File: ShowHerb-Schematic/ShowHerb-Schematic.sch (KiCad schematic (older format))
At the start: 7 parts

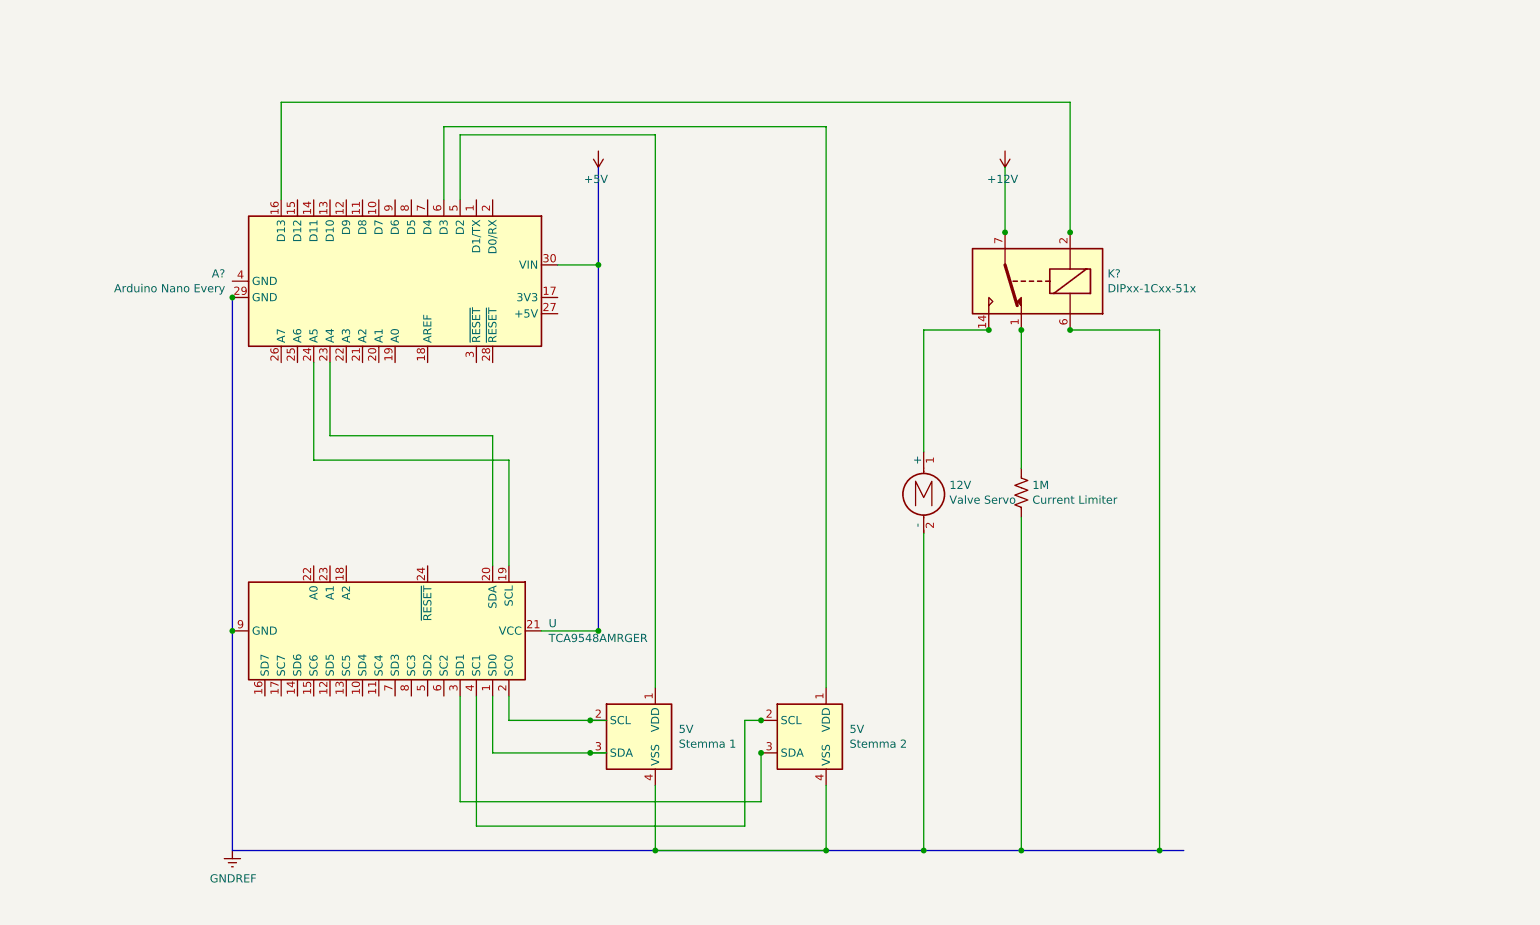
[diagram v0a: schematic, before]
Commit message: Added rain sensor and photoresistor to schematic, v2 storage box
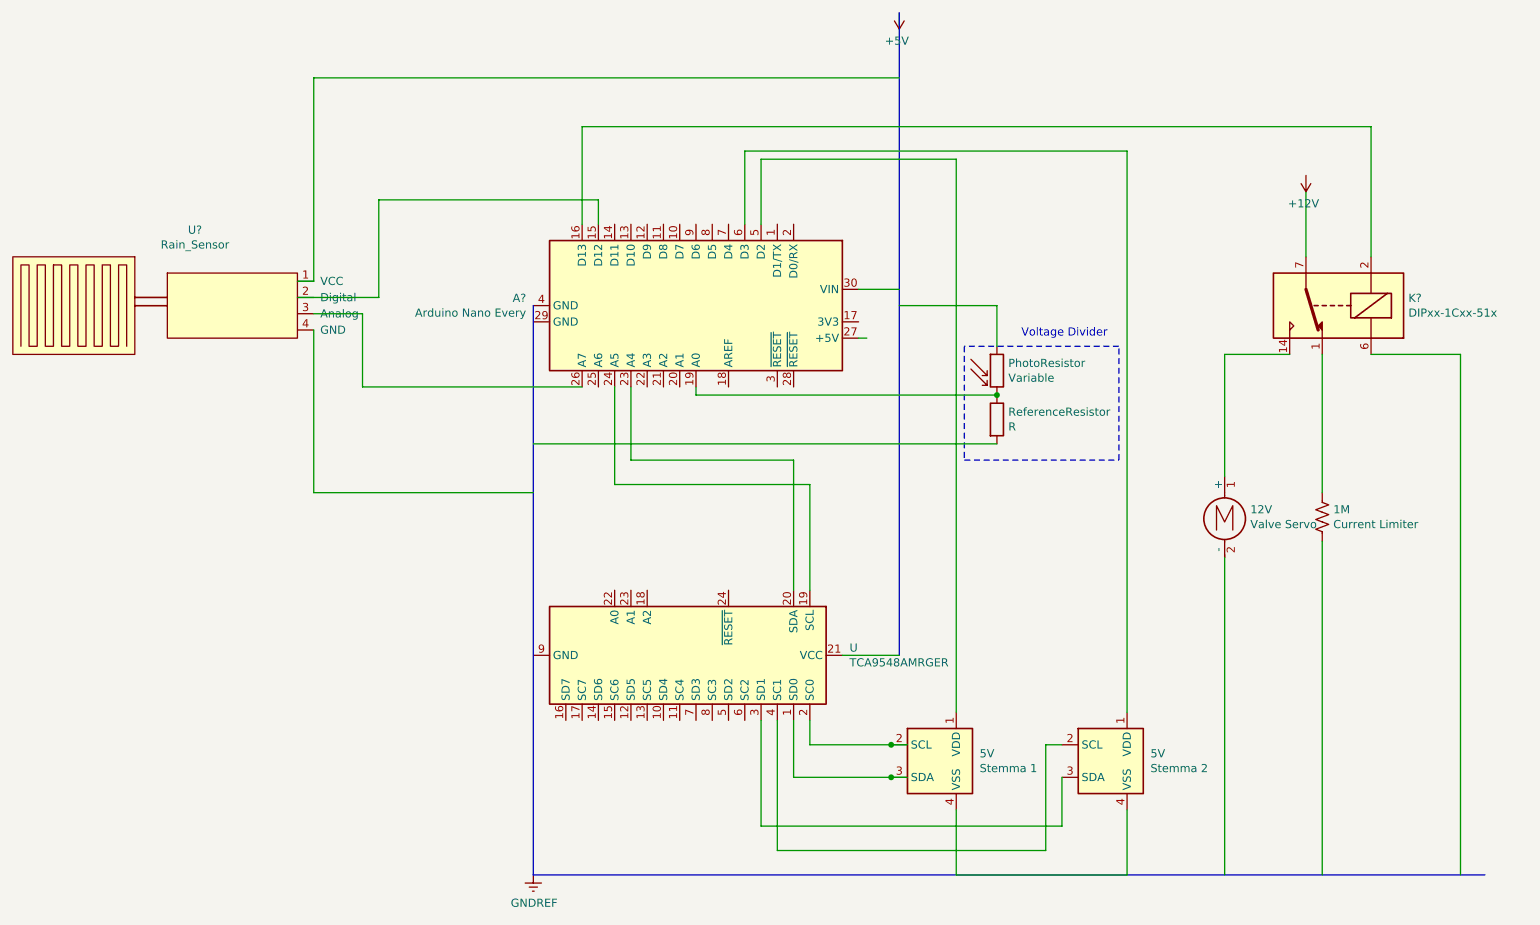
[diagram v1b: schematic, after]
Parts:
- added PhotoResistor: Variable, symbol Device:R_PHOTO
- added ReferenceResistor: R, symbol Device:R
- added U?: Rain_Sensor, symbol RainSensor:Rain_Sensor
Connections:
- wire segments 41 -> 59
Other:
- note added: "Voltage Divider\n"
- moved on the sheet: 12V, 1M, 5V, A?, K?, U
